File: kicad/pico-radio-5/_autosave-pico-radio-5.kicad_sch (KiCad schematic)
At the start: 6 parts, among them U1 SI4732-A10-GS, U2 TFT_320x240, U3 KY-040, Y1 Crystal

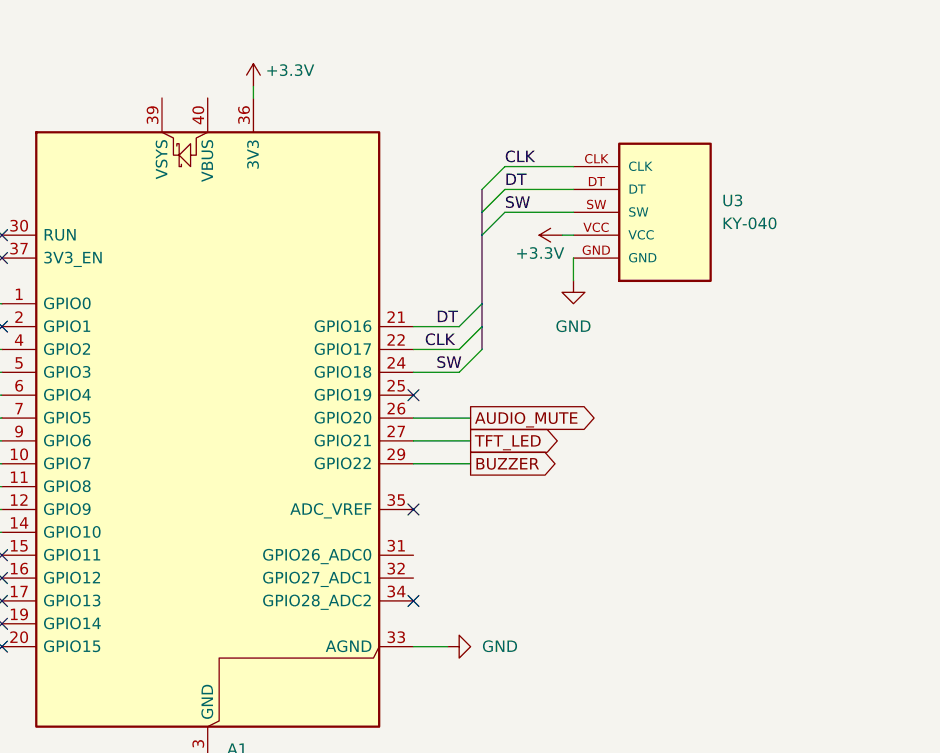
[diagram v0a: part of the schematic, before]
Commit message: Add PicoSensorUtils for voltage and temperature readings
- Implemented initialization function for ADC.
- Added function to read VSYS voltage from ADC3 with caching mechanism.
- Added function to read core temperature from ADC0 with caching mechanism.
- Implemented cache clearing function to reset sensor values.
- Prepared structure for potential cache status query (commented out).
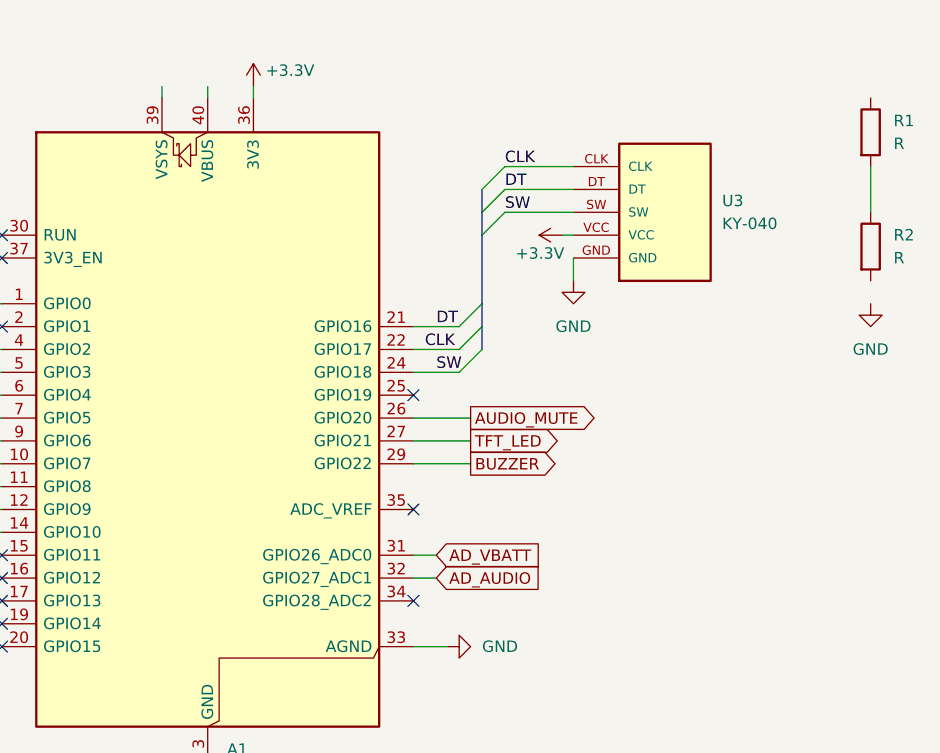
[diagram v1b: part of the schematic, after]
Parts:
- added R1, R2: R, symbol Device:R
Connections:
- net AD_VBATT: now reaches A1.31 (GPIO26_ADC0)
- net AD_AUDIO: now reaches A1.32 (GPIO27_ADC1)
- new net: R1.2, R2.1
